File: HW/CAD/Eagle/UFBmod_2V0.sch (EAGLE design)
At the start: 184 parts, among them T0551 MMBT2222, U0501 MIDAS_MCCOG21605B6W-FPTLWI, U0601 MAX5217, U0701 AT86RF215-ZU, U0711 ASVTX-13-D-26.000MHZ-I05-T, U0811 PE4259, U0821 RFX1010, U0881 B39871B3440U410, U0911 FT232HL, U1101 TPS53353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

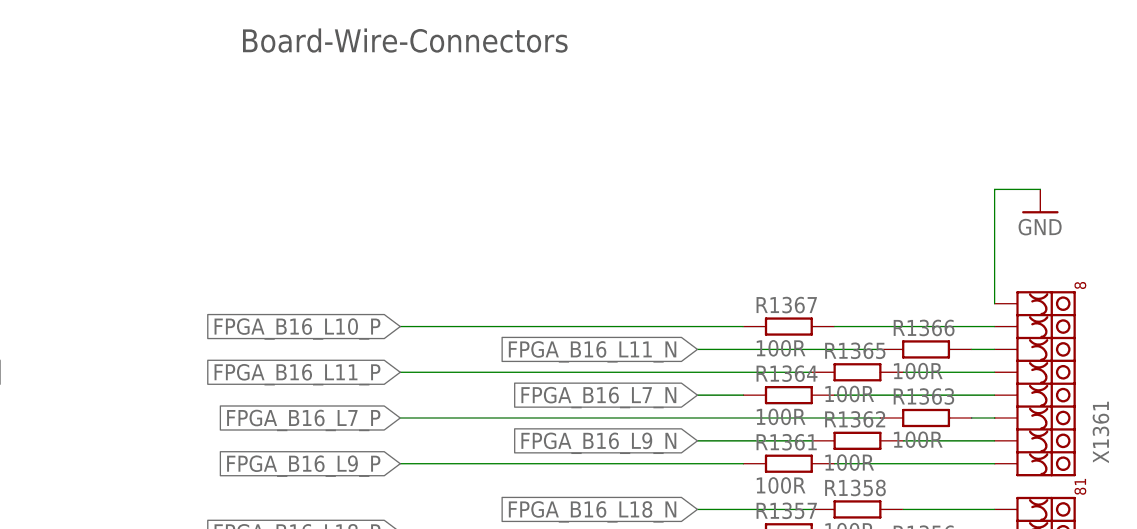
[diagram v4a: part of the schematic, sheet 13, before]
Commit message: HW_2V0 - HW/CAD/Eagle - routing of PMIC 3.3V done
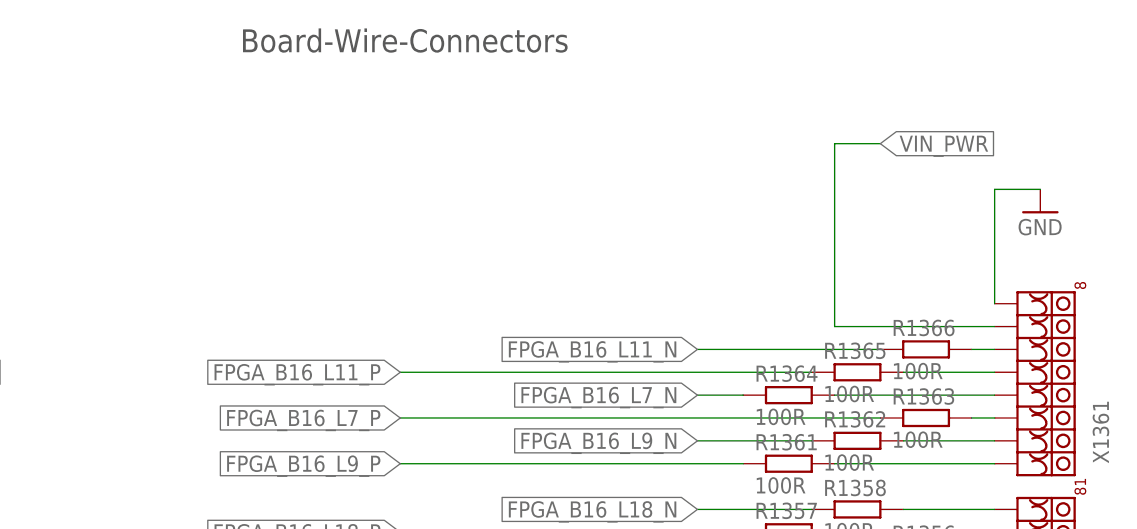
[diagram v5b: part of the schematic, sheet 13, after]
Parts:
- removed R1367: 100R, df4iah_rcl:R-EU_R0402
- D0971: value GREEN -> CMD17-21VGD/TR8 GREEN; device df4iah_led:U57X32 -> df4iah_led:LEDCHIP-LED0805
- D0972: value RED -> CMD17-21VRD/TR8 RED; device df4iah_led:U57X32 -> df4iah_led:LEDCHIP-LED0805
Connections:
- removed net B2W_67: R1367.2, X1361.7
- net FPGA_B16_L10_P: no longer R1367.1
- net VIN_PWR: now also X1361.7
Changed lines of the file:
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@@
 <part name="R0971" library="df4iah_rcl" deviceset="R-EU_" device="R0402" value="1kR"/>
 <part name="R0972" library="df4iah_rcl" deviceset="R-EU_" device="R0402" value="1kR"/>
-<part name="D0972" library="df4iah_led" deviceset="U57X32" device="" value="RED"/>
-<part name="D0971" library="df4iah_led" deviceset="U57X32" device="" value="GREEN"/>
+<part name="D0972" library="df4iah_led" deviceset="LED" device="CHIP-LED0805" value="CMD17-21VRD/TR8  RED"/>
+<part name="D0971" library="df4iah_led" deviceset="LED" device="CHIP-LED0805" value="CMD17-21VGD/TR8  GREEN"/>
 <part name="X1331" library="df4iah_connector" deviceset="XILINX-JTAG-14" device=""/>
 <part name="R1351" library="df4iah_rcl" deviceset="R-EU_" device="R0402" value="100R"/>
@@
 <part name="R1365" library="df4iah_rcl" deviceset="R-EU_" device="R0402" value="100R"/>
 <part name="R1366" library="df4iah_rcl" deviceset="R-EU_" device="R0402" value="100R"/>
-<part name="R1367" library="df4iah_rcl" deviceset="R-EU_" device="R0402" value="100R"/>
 <part name="X1350" library="df4iah_connector" deviceset="HEADER-2X3" device=""/>
 <part name="+2V5_1350" library="df4iah_supply" deviceset="+2V5" device=""/>
@@
 </segment>
 </net>
-<net name="FPGA_ETH_TD_P" class="0">
+<net name="FPGA_ETH_TD_P" class="3">
 <segment>
 <pinref part="JB1" gate="G$1" pin="ETH_TD_P"/>
@@
 </segment>
 </net>
-<net name="FPGA_ETH_TD_N" class="0">
+<net name="FPGA_ETH_TD_N" class="3">
 <segment>
 <pinref part="JB1" gate="G$1" pin="ETH_TD_N"/>
@@
 </segment>
 </net>
-<net name="FPGA_ETH_RD_P" class="0">
+<net name="FPGA_ETH_RD_P" class="3">
 <segment>
 <pinref part="JB1" gate="G$1" pin="ETH_RD_P"/>
@@
 </segment>
 </net>
-<net name="FPGA_ETH_RD_N" class="0">
+<net name="FPGA_ETH_RD_N" class="3">
 <segment>
 <pinref part="JB1" gate="G$1" pin="ETH_RD_N"/>
@@
 </segment>
 </net>
-<net name="FPGA_B16_L16_P" class="0">
+<net name="FPGA_B16_L16_P" class="3">
 <segment>
 <pinref part="JB1" gate="G$1" pin="B16_L16_P"/>
@@
 </segment>
 </net>
-<net name="FPGA_B16_L16_N" class="0">
+<net name="FPGA_B16_L16_N" class="3">
 <segment>
 <pinref part="JB1" gate="G$1" pin="B16_L16_N"/>
@@
 </segment>
 </net>
-<net name="FPGA_B16_L19_N" class="0">
+<net name="FPGA_B16_L19_N" class="3">
 <segment>
 <pinref part="JB1" gate="G$1" pin="B16_L19_N"/>
@@
 </segment>
 </net>
-<net name="FPGA_B16_L19_P" class="0">
+<net name="FPGA_B16_L19_P" class="3">
 <segment>
 <pinref part="JB1" gate="G$1" pin="B16_L19_P"/>
@@
 </segment>
 </net>
-<net name="FPGA_B16_L17_N" class="0">
+<net name="FPGA_B16_L17_N" class="3">
 <segment>
 <pinref part="JB1" gate="G$1" pin="B16_L17_N"/>
@@
 </segment>
 </net>
-<net name="FPGA_B16_L17_P" class="0">
+<net name="FPGA_B16_L17_P" class="3">
 <segment>
 <pinref part="JB1" gate="G$1" pin="B16_L17_P"/>
@@
 </segment>
 </net>
-<net name="FPGA_B16_L18_N" class="0">
+<net name="FPGA_B16_L18_N" class="3">
 <segment>
 <pinref part="JB1" gate="G$1" pin="B16_L18_N"/>
@@
 </segment>
 </net>
-<net name="FPGA_B16_L18_P" class="0">
+<net name="FPGA_B16_L18_P" class="3">
 <segment>
 <pinref part="JB1" gate="G$1" pin="B16_L18_P"/>
@@
 </segment>
 </net>
-<net name="FPGA_B16_L7_N" class="0">
+<net name="FPGA_B16_L7_N" class="3">
 <segment>
 <pinref part="JB1" gate="G$1" pin="B16_L7_N"/>
@@
 </segment>
 </net>
-<net name="FPGA_B16_L7_P" class="0">
+<net name="FPGA_B16_L7_P" class="3">
 <segment>
 <pinref part="JB1" gate="G$1" pin="B16_L7_P"/>
@@
 </segment>
 </net>
-<net name="FPGA_B16_L11_P" class="0">
+<net name="FPGA_B16_L11_P" class="3">
 <segment>
 <pinref part="JB1" gate="G$1" pin="B16_L11_P"/>
@@
 </segment>
 </net>
-<net name="FPGA_B16_L11_N" class="0">
+<net name="FPGA_B16_L11_N" class="3">
 <segment>
 <pinref part="JB1" gate="G$1" pin="B16_L11_N"/>
@@
 </segment>
 </net>
-<net name="FPGA_B16_L9_N" class="0">
+<net name="FPGA_B16_L9_N" class="3">
 <segment>
 <pinref part="JB1" gate="G$1" pin="B16_L9_N"/>
@@
 </segment>
 </net>
-<net name="FPGA_B16_L9_P" class="0">
+<net name="FPGA_B16_L9_P" class="3">
 <segment>
 <pinref part="JB1" gate="G$1" pin="B16_L9_P"/>
@@
 <instance part="R0971" gate="G$1" x="175.26" y="96.52"/>
 <instance part="R0972" gate="G$1" x="182.88" y="93.98"/>
-<instance part="D0972" gate="1" x="193.04" y="86.36"/>
-<instance part="D0971" gate="1" x="205.74" y="86.36"/>
+<instance part="D0972" gate="G$1" x="193.04" y="86.36"/>
+<instance part="D0971" gate="G$1" x="205.74" y="86.36"/>
 </instances>
 <busses>
@@
 <wire x1="124.46" y1="38.1" x2="193.04" y2="38.1" width="0.1524" layer="91"/>
 <junction x="124.46" y="38.1"/>
-<pinref part="D0971" gate="1" pin="C"/>
+<pinref part="D0971" gate="G$1" pin="C"/>
 <wire x1="193.04" y1="38.1" x2="205.74" y2="38.1" width="0.1524" layer="91"/>
 <wire x1="205.74" y1="38.1" x2="205.74" y2="81.28" width="0.1524" layer="91"/>
-<pinref part="D0972" gate="1" pin="C"/>
+<pinref part="D0972" gate="G$1" pin="C"/>
 <wire x1="193.04" y1="38.1" x2="193.04" y2="81.28" width="0.1524" layer="91"/>
 <junction x="193.04" y="38.1"/>
@@
 <wire x1="187.96" y1="93.98" x2="193.04" y2="93.98" width="0.1524" layer="91"/>
 <wire x1="193.04" y1="93.98" x2="193.04" y2="88.9" width="0.1524" layer="91"/>
-<pinref part="D0972" gate="1" pin="A"/>
+<pinref part="D0972" gate="G$1" pin="A"/>
 </segment>
 </net>
@@
 <wire x1="180.34" y1="96.52" x2="205.74" y2="96.52" width="0.1524" layer="91"/>
 <wire x1="205.74" y1="96.52" x2="205.74" y2="88.9" width="0.1524" layer="91"/>
-<pinref part="D0971" gate="1" pin="A"/>
+<pinref part="D0971" gate="G$1" pin="A"/>
 </segment>
 </net>
@@
 <instance part="R1365" gate="G$1" x="228.6" y="127"/>
 <instance part="R1366" gate="G$1" x="236.22" y="129.54"/>
-<instance part="R1367" gate="G$1" x="220.98" y="132.08"/>
 <instance part="X1350" gate="G$1" x="223.52" y="55.88"/>
 <instance part="+2V5_1350" gate="G$2" x="175.26" y="43.18" rot="R90"/>
@@
 </segment>
 </net>
-<net name="B2W_67" class="0">
+<net name="VIN_PWR" class="0">
 <segment>
 <pinref part="X1361" gate="G$1" pin="7"/>
 <wire x1="243.84" y1="132.08" x2="226.06" y2="132.08" width="0.1524" layer="91"/>
-<pinref part="R1367" gate="G$1" pin="2"/>
+<wire x1="226.06" y1="132.08" x2="226.06" y2="152.4" width="0.1524" layer="91"/>
+<wire x1="226.06" y1="152.4" x2="231.14" y2="152.4" width="0.1524" layer="91"/>
+<label x="231.14" y="152.4" size="1.778" layer="95" xref="yes"/>
 </segment>
 </net>
-<net name="FPGA_B16_L16_P" class="0">
+<net name="FPGA_B16_L16_P" class="3">
 <segment>
 <pinref part="R1351" gate="G$1" pin="1"/>
@@
 </segment>
 </net>
-<net name="FPGA_B16_L16_N" class="0">
+<net name="FPGA_B16_L16_N" class="3">
 <segment>
 <pinref part="R1352" gate="G$1" pin="1"/>
@@
 </segment>
 </net>
-<net name="FPGA_B16_L19_P" class="0">
+<net name="FPGA_B16_L19_P" class="3">
 <segment>
 <pinref part="R1353" gate="G$1" pin="1"/>
@@
 </segment>
 </net>
-<net name="FPGA_B16_L19_N" class="0">
+<net name="FPGA_B16_L19_N" class="3">
 <segment>
 <pinref part="R1354" gate="G$1" pin="1"/>
@@
 </segment>
 </net>
-<net name="FPGA_B16_L17_P" class="0">
+<net name="FPGA_B16_L17_P" class="3">
 <segment>
 <pinref part="R1355" gate="G$1" pin="1"/>
@@
 </segment>
 </net>
-<net name="FPGA_B16_L17_N" class="0">
+<net name="FPGA_B16_L17_N" class="3">
 <segment>
 <pinref part="R1356" gate="G$1" pin="1"/>
@@
 </segment>
 </net>
-<net name="FPGA_B16_L18_P" class="0">
+<net name="FPGA_B16_L18_P" class="3">
 <segment>
 <pinref part="R1357" gate="G$1" pin="1"/>
@@
 </segment>
 </net>
-<net name="FPGA_B16_L18_N" class="0">
+<net name="FPGA_B16_L18_N" class="3">
 <segment>
 <pinref part="R1358" gate="G$1" pin="1"/>
@@
 </segment>
 </net>
-<net name="FPGA_B16_L7_P" class="0">
+<net name="FPGA_B16_L7_P" class="3">
 <segment>
 <pinref part="R1363" gate="G$1" pin="1"/>
@@
 </segment>
 </net>
-<net name="FPGA_B16_L7_N" class="0">
+<net name="FPGA_B16_L7_N" class="3">
 <segment>
 <pinref part="R1364" gate="G$1" pin="1"/>
@@
 </segment>
 </net>
-<net name="FPGA_B16_L11_P" class="0">
+<net name="FPGA_B16_L11_P" class="3">
 <segment>
 <pinref part="R1365" gate="G$1" pin="1"/>
@@
 </segment>
 </net>
-<net name="FPGA_B16_L11_N" class="0">
+<net name="FPGA_B16_L11_N" class="3">
 <segment>
 <pinref part="R1366" gate="G$1" pin="1"/>
@@
 </segment>
 </net>
-<net name="FPGA_B16_L10_P" class="0">
-<segment>
-<pinref part="R1367" gate="G$1" pin="1"/>
-<wire x1="215.9" y1="132.08" x2="177.8" y2="132.08" width="0.1524" layer="91"/>
-<label x="177.8" y="132.08" size="1.778" layer="95" rot="R180" xref="yes"/>
-</segment>
-</net>
-<net name="FPGA_B16_L9_P" class="0">
+<net name="FPGA_B16_L9_P" class="3">
 <segment>
 <pinref part="R1361" gate="G$1" pin="1"/>
@@
 </segment>
 </net>
-<net name="FPGA_B16_L9_N" class="0">
+<net name="FPGA_B16_L9_N" class="3">
 <segment>
 <pinref part="R1362" gate="G$1" pin="1"/>
@@
 </segment>
 </net>
-<net name="FPGA_ETH_TD_P" class="0">
+<net name="FPGA_ETH_TD_P" class="3">
 <segment>
 <pinref part="J1411" gate="G$1" pin="3"/>
@@
 </segment>
 </net>
-<net name="FPGA_ETH_RD_P" class="0">
+<net name="FPGA_ETH_RD_P" class="3">
 <segment>
 <pinref part="J1411" gate="G$1" pin="7"/>
@@
 </segment>
 </net>
-<net name="FPGA_ETH_TD_N" class="0">
+<net name="FPGA_ETH_TD_N" class="3">
 <segment>
 <pinref part="J1411" gate="G$1" pin="4"/>
@@
 </segment>
 </net>
-<net name="FPGA_ETH_RD_N" class="0">
+<net name="FPGA_ETH_RD_N" class="3">
 <segment>
 <pinref part="J1411" gate="G$1" pin="8"/>

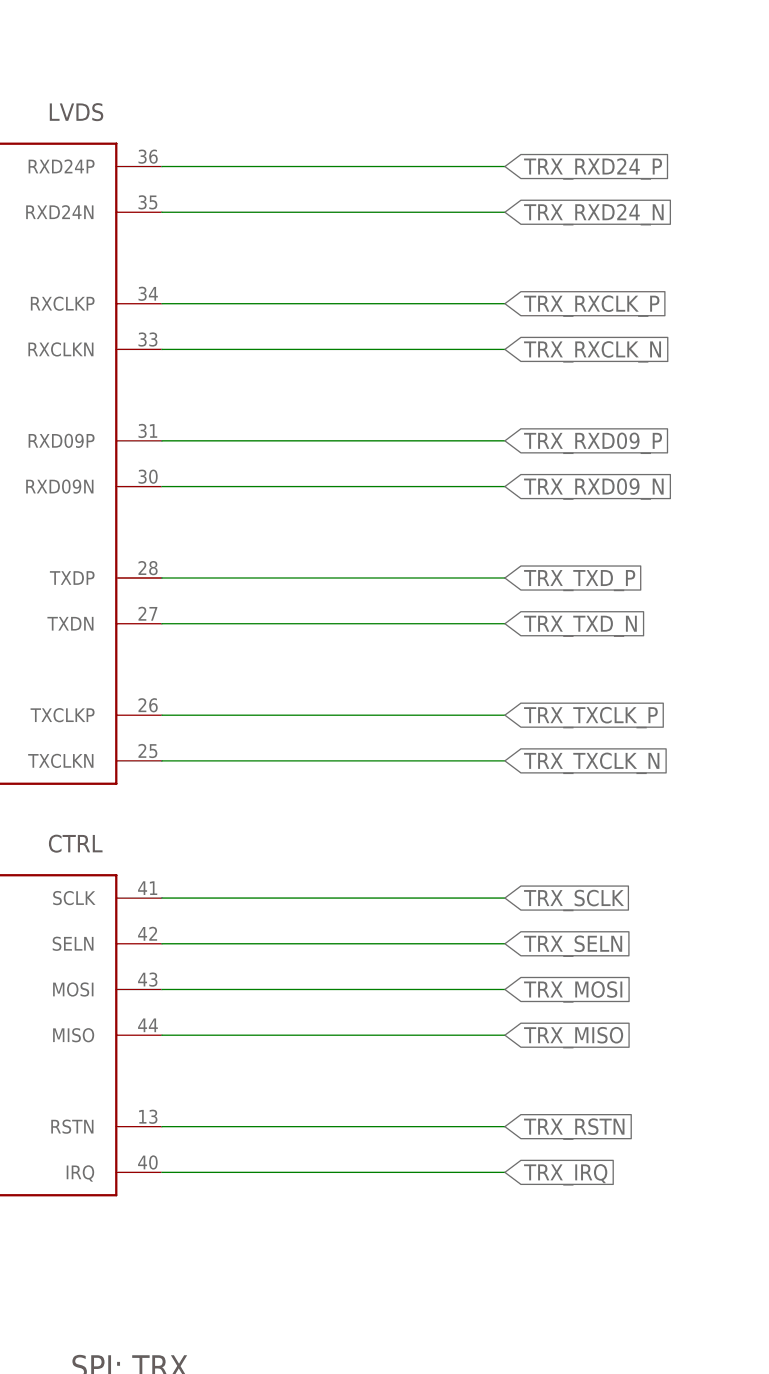
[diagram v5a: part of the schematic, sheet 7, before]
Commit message: HW_2V0 - HW/CAD/Eagle - LVDS traces to TRX added
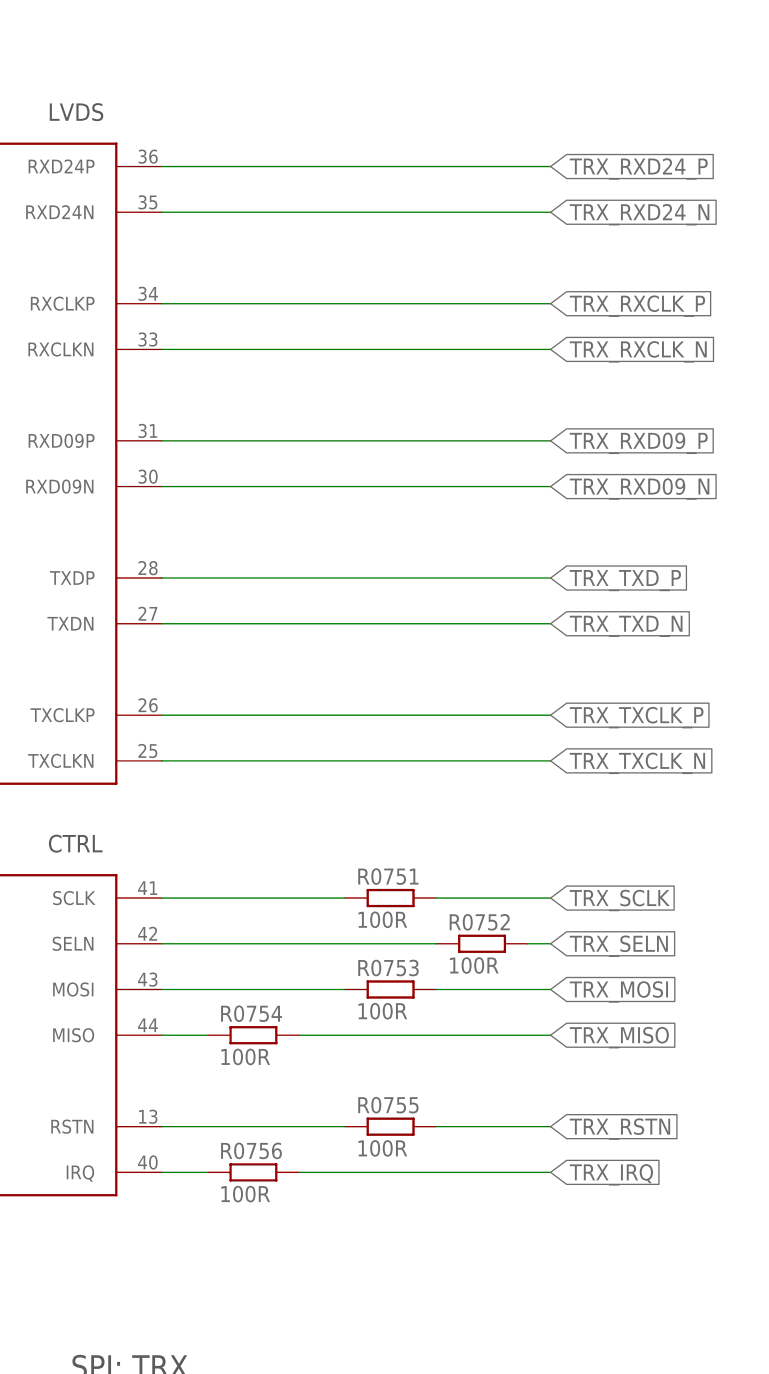
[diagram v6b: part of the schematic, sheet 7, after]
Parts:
- added R0751, R0752, R0753, R0754, R0755, R0756: 100R, df4iah_rcl:R-EU_R0402
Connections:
- new net TRX_IRQ_R: R0756.1, U0701.IRQ
- new net TRX_MISO_R: R0754.1, U0701.MISO
- new net TRX_MOSI_R: R0753.1, U0701.MOSI
- new net TRX_RSTN_R: R0755.1, U0701.RSTN
- new net TRX_SCLK_R: R0751.1, U0701.SCLK
- new net TRX_SELN_R: R0752.1, U0701.SELN
- net TRX_IRQ: now also JB2.B15_L16_N, R0756.2; no longer U0701.IRQ
- net TRX_MISO: now also JB2.B15_L2_P, R0754.2; no longer U0701.MISO
- net TRX_MOSI: now also JB2.B15_L2_N, R0753.2; no longer U0701.MOSI
- net TRX_RSTN: now also JB2.B15_L16_P, R0755.2; no longer U0701.RSTN
- net TRX_SCLK: now also JB2.B15_L1_P, R0751.2; no longer U0701.SCLK
- net TRX_SELN: now also JB2.B15_L1_N, R0752.2; no longer U0701.SELN

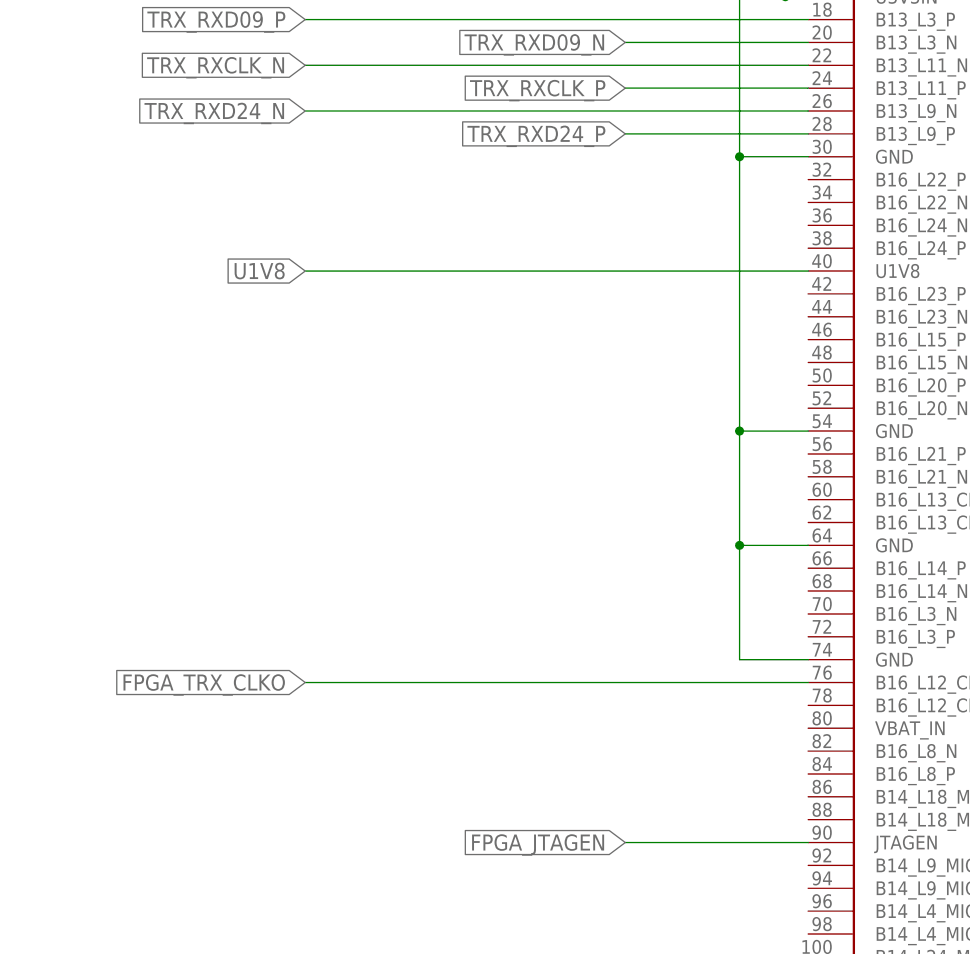
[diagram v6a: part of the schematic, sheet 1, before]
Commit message: HW - CAD/Eagle - RGB-LED and LCD backlight connected
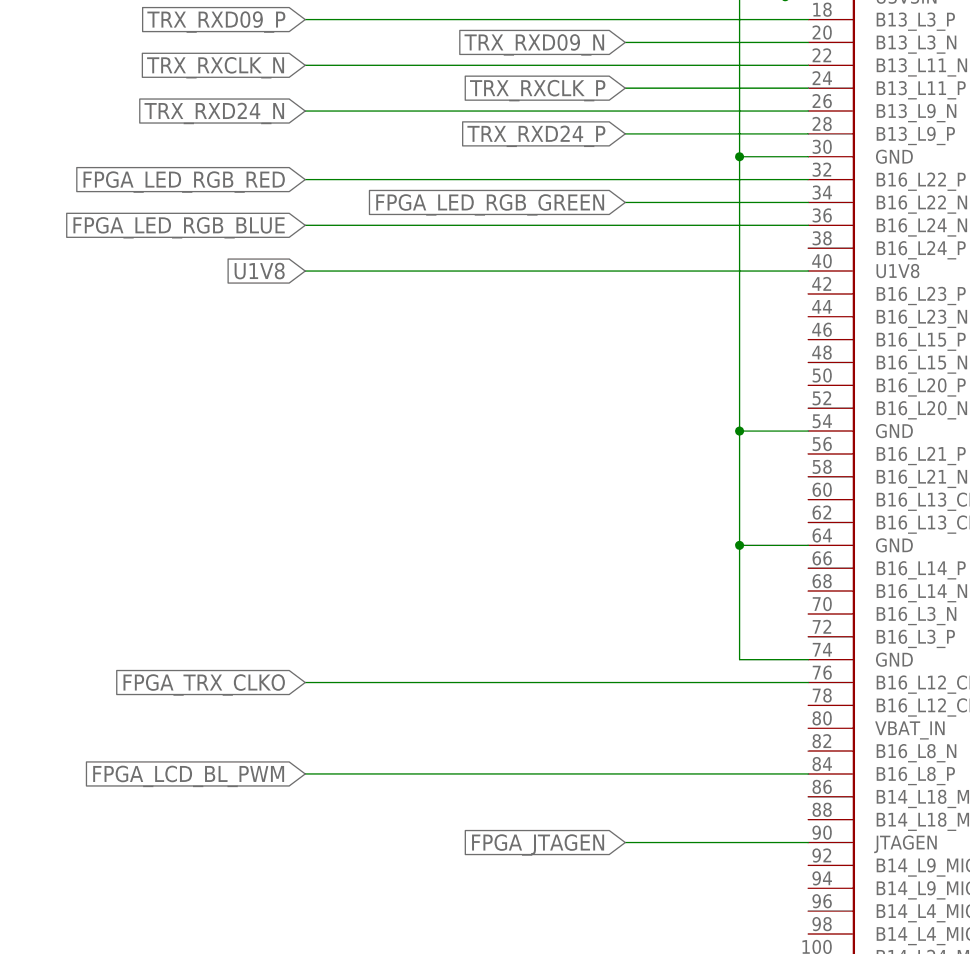
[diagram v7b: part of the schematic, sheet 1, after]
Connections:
- net FPGA_LCD_BL_PWM: now also JB1.B16_L8_P
- net FPGA_LED_RGB_BLUE: now also JB1.B16_L24_N
- net FPGA_LED_RGB_GREEN: now also JB1.B16_L22_N
- net FPGA_LED_RGB_RED: now also JB1.B16_L22_P
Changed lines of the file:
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@@
+</segment>
+</net>
+<net name="FPGA_LED_RGB_RED" class="0">
+<segment>
+<pinref part="JB1" gate="G$1" pin="B16_L22_P"/>
+<wire x1="96.52" y1="114.3" x2="40.64" y2="114.3" width="0.1524" layer="91"/>
+<label x="40.64" y="114.3" size="1.778" layer="95" rot="R180" xref="yes"/>
+</segment>
+</net>
+<net name="FPGA_LED_RGB_GREEN" class="0">
+<segment>
+<pinref part="JB1" gate="G$1" pin="B16_L22_N"/>
+<wire x1="96.52" y1="111.76" x2="76.2" y2="111.76" width="0.1524" layer="91"/>
+<label x="76.2" y="111.76" size="1.778" layer="95" rot="R180" xref="yes"/>
+</segment>
+</net>
+<net name="FPGA_LED_RGB_BLUE" class="0">
+<segment>
+<pinref part="JB1" gate="G$1" pin="B16_L24_N"/>
+<wire x1="96.52" y1="109.22" x2="40.64" y2="109.22" width="0.1524" layer="91"/>
+<label x="40.64" y="109.22" size="1.778" layer="95" rot="R180" xref="yes"/>
+</segment>
+</net>
+<net name="FPGA_LCD_BL_PWM" class="0">
+<segment>
+<pinref part="JB1" gate="G$1" pin="B16_L8_P"/>
+<wire x1="96.52" y1="48.26" x2="40.64" y2="48.26" width="0.1524" layer="91"/>
+<label x="40.64" y="48.26" size="1.778" layer="95" rot="R180" xref="yes"/>
 </segment>
 </net>
